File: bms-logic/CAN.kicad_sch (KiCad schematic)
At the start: 56 parts, among them J5 Connector, USB-TYPE-C-16P, J6 Conn_01x04, U10 TCAN334D, U5 MP9485GN-Z, U6 MIE1W0505BGLVH-3R-Z, U7 ISO7041FDBQ, U8 ADUM3160, U9 LTV-217-B-G

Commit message: started afe layout
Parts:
- renumbered C22 to C18, C23 to C19, C24 to C20, C25 to C21, C26 to C22, C27 to C23, C28 to C24, C29 to C25, C30 to C26, C31 to C27, C32 to C28, C33 to C29, C34 to C30, C35 to C31, C36 to C32, C37 to C33, C38 to C34, C39 to C35, J5 to J3, J6 to J4, U8 to U10, U9 to U11, U10 to U12, U5 to U7, U6 to U8, U7 to U9

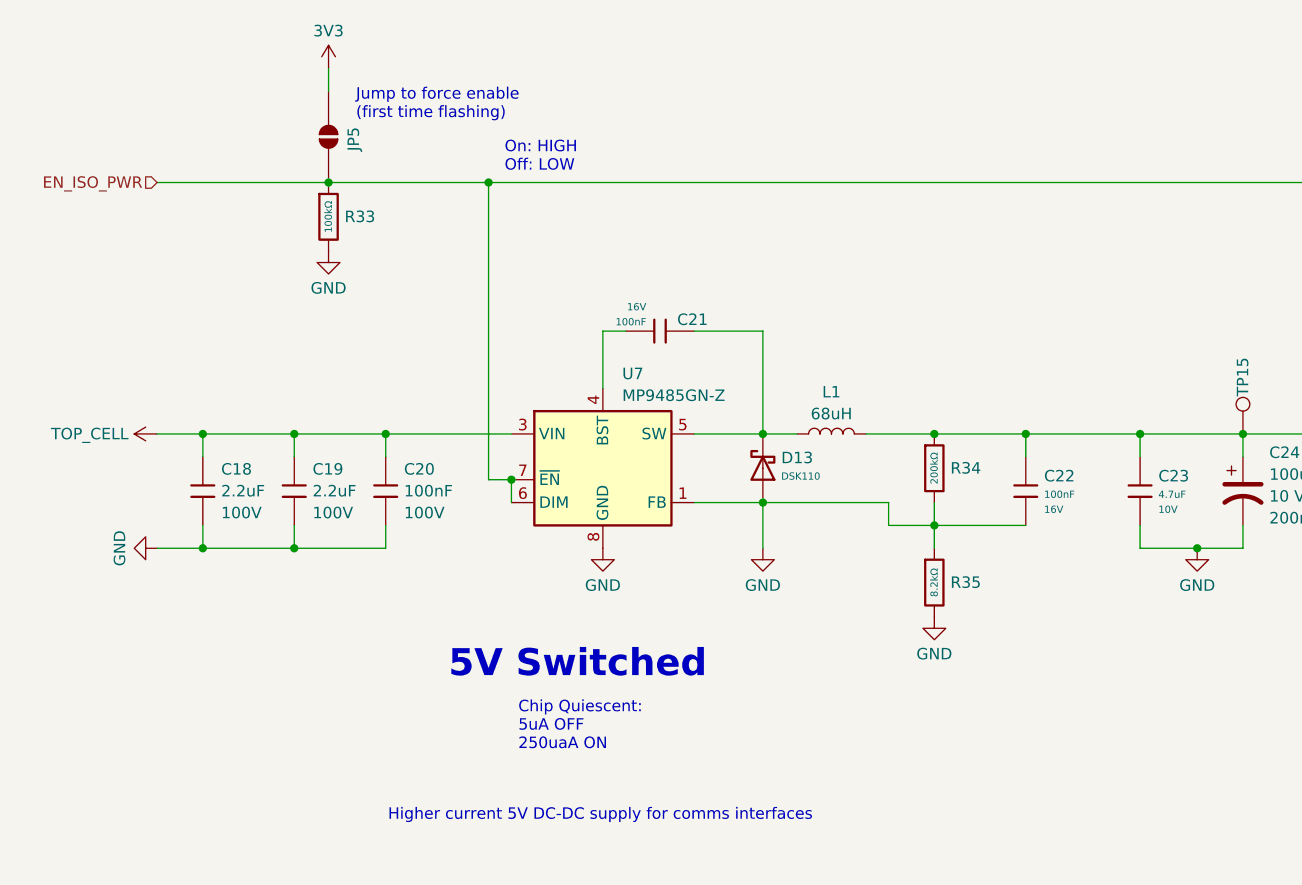
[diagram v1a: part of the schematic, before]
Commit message: power supply layout
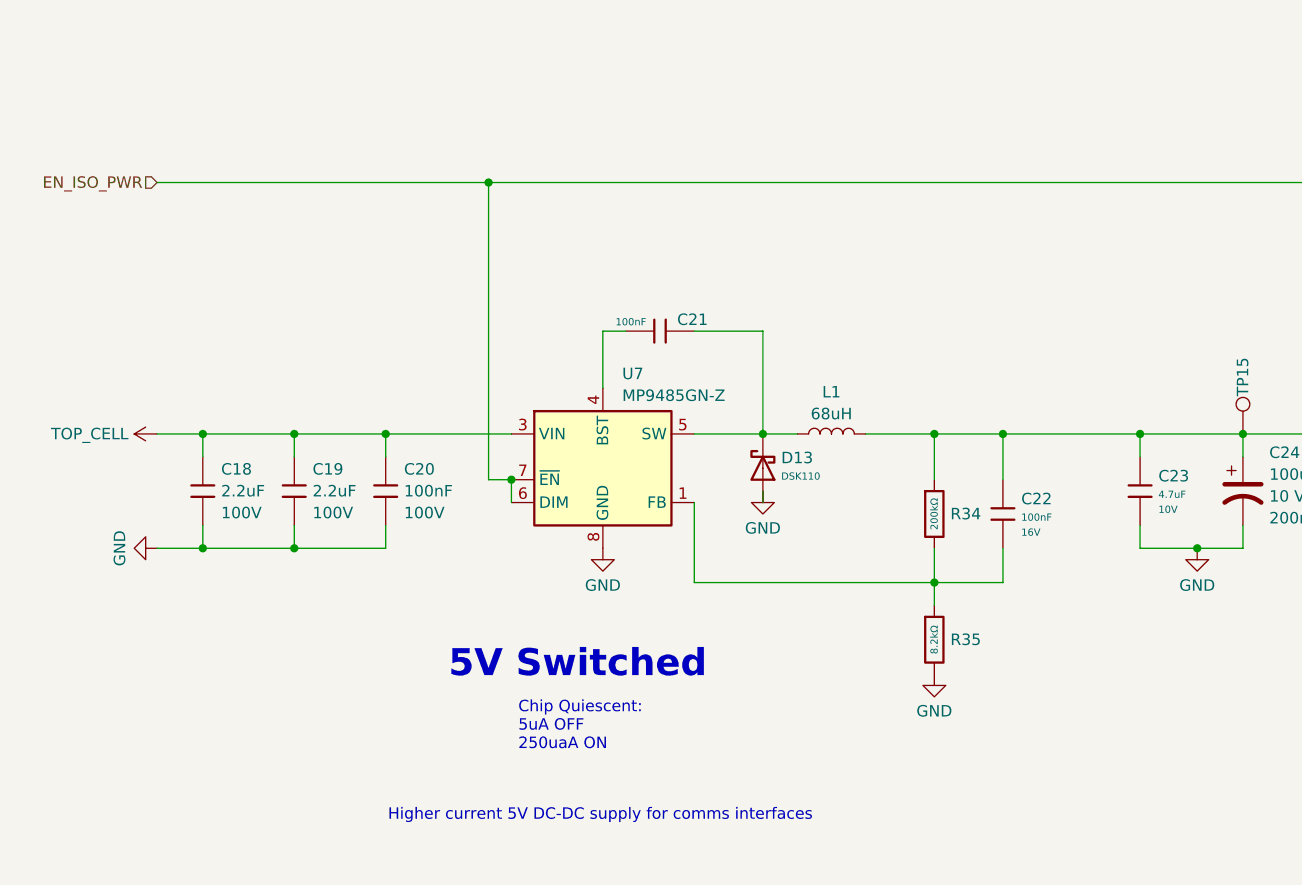
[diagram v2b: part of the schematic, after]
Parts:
- removed JP5: SolderJumper_2_Open, Jumper:SolderJumper-2_P1.3mm_Open_RoundedPad1.0x1.5mm, symbol Jumper:SolderJumper_2_Open
- removed R33: 100kΩ, PCM_JLCPCB:R_0402, symbol PCM_JLCPCB-Resistors:0402,100kΩ
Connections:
- net GND: no longer C22.1, R34.2, R35.1, U7.1 (FB)
- new net: C22.1, R34.2, R35.1, U7.1 (FB)
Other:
- note removed: "Jump to force enable (first time flashing)"
- note removed: "On: HIGH Off: LOW"
- moved on the sheet: C22, R34, R35

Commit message: isolated comms
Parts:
- removed J4: Conn_01x04, symbol Connector_Generic:Conn_01x04
- removed JP6: SolderJumper_2_Open, Jumper:SolderJumper-2_P1.3mm_Open_RoundedPad1.0x1.5mm, symbol Jumper:SolderJumper_2_Open
- added C54, C55: 100nF, PCM_JLCPCB:C_0402, symbol PCM_JLCPCB-Capacitors:0402,100nF
- added CN5: S4B-ZR-SM4A-TF_LF_SN, Connector_JST:JST_ZH_S4B-ZR-SM4A-TF_1x04-1MP_P1.50mm_Horizontal, symbol JLCImport:S4B-ZR-SM4A-TF_LF_SN
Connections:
- net 3V3: now also C54.1
- net 5V0_ISO_SW: now also C55.1, CN5.1
- net GND: now also C54.2; no longer C31.1
- net GNDISO: now also C31.1, C55.2, CN5.4, CN5.5, CN5.6
- net at D15.1 (K), R47.1, U12.7 (CANH): now also CN5.2
- net at D15.2 (K), JP7.1 (A), U12.6 (CANL): now also CN5.3
- no-connect marks 5 -> 6
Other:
- moved on the sheet: TP16, TP17, TP18, TP19

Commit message: diagonal
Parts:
- CN5: footprint Connector_JST:JST_ZH_S4B-ZR-SM4A-TF_1x04-1MP_P1.50mm_Horizontal -> JLCImport:JST_ZH_S4B-ZR-SM4A-TF_1x04-1MP_P1.50mm_Horizontal
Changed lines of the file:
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@@
 			)
 		)
-		(property "Footprint" "Connector_JST:JST_ZH_S4B-ZR-SM4A-TF_1x04-1MP_P1.50mm_Horizontal"
+		(property "Footprint" "JLCImport:JST_ZH_S4B-ZR-SM4A-TF_1x04-1MP_P1.50mm_Horizontal"
 			(at 388.62 119.38 0)
 			(hide yes)

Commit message: kicad 10.0.1 before update to .2
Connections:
- net GNDISO: now also CN5.MP (5); no longer CN5.5, CN5.6
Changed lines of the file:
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@@
 		(pin "3"
 		)
-		(pin "6"
+		(pin "MP"
 		)
 		(pin "2"
@@
 		(pin "1"
 		)
-		(pin "5"
+		(pin "MP"
 		)
 		(instances

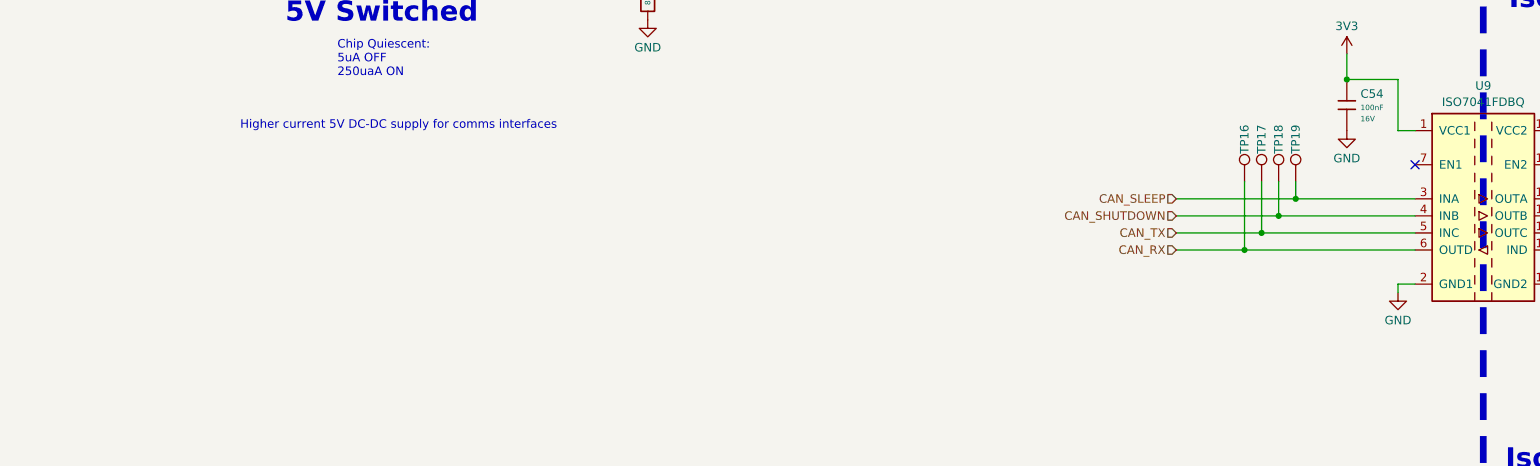
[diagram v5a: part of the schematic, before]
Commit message: more layout, removed some unnecessary features
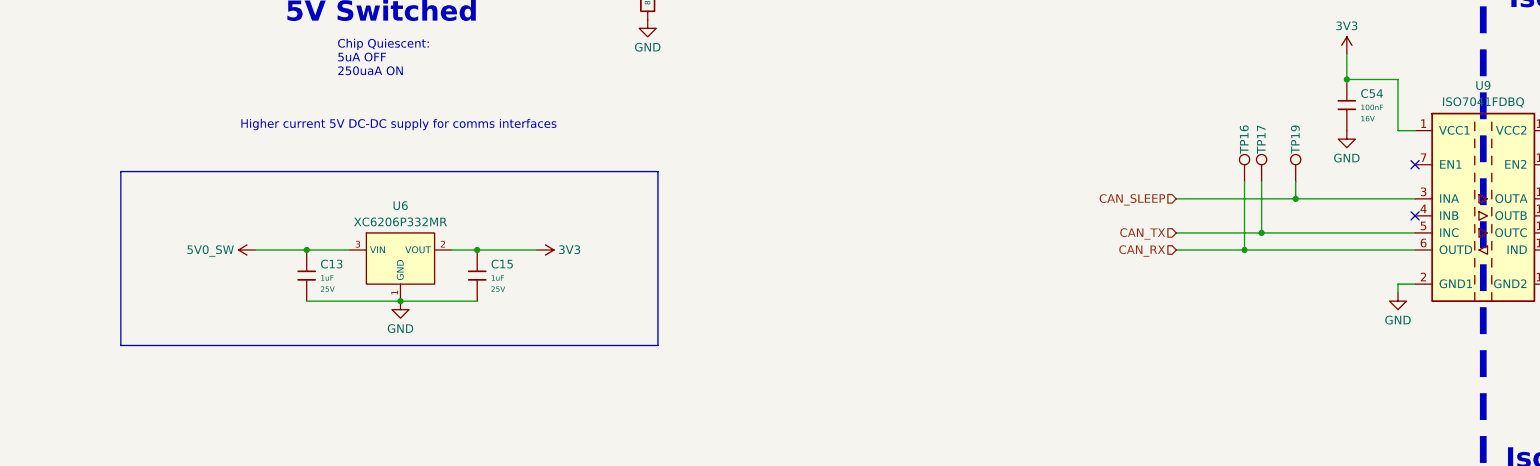
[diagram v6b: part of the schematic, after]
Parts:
- removed TP18: IO8, TestPoint:TestPoint_Pad_D1.0mm, symbol Connector:TestPoint
- added C13, C15: 1uF, PCM_JLCPCB:C_0402, symbol PCM_JLCPCB-Capacitors:0402,1uF
- added U6: XC6206P332MR, PCM_JLCPCB:SOT-23-3_L2.9-W1.6-P1.90-LS2.8-BR, symbol PCM_JLCPCB-Power:LDO, 3.3V, 0.2A
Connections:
- net 3V3: now also C15.1, U6.2 (VOUT)
- net 5V0_SW: now also C13.1, U6.3 (VIN)
- net GND: now also C13.2, C15.2, U6.1 (GND)
- net CAN_SHUTDOWN: no longer names the net of U9.4 (INB)
- no-connect marks 6 -> 7

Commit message: done with layout, need to address some DRC
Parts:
- renumbered CN5 to CN7, J3 to CN8
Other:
- note added: "change sch symbool to CN?"
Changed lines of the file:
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@@
 		)
 	)
+	(text "change sch symbool to CN?"
+		(exclude_from_sim no)
+		(at 357.632 184.658 0)
+		(effects
+			(font
+				(size 1.27 1.27)
+			)
+		)
+	)
 	(text "Isolated CANbus 2.0B Interface"
 		(exclude_from_sim no)
@@
 		(in_pos_files yes)
 		(dnp no)
-		(property "Reference" "CN5"
+		(property "Reference" "CN7"
 			(at 378.714 135.4977 0)
 			(show_name no)
@@
 			(project "battery-node"
 				(path "/0531bb65-44fe-462a-8fbf-92fb22c9abe0/a0e287d3-b915-410a-86a7-dfb59e4205a2"
-					(reference "CN5")
+					(reference "CN7")
 					(unit 1)
 				)
@@
 		(in_pos_files yes)
 		(dnp no)
-		(property "Reference" "J3"
+		(property "Reference" "CN8"
 			(at 328.93 176.0799 0)
 			(show_name no)
@@
 			(project "battery-node"
 				(path "/0531bb65-44fe-462a-8fbf-92fb22c9abe0/a0e287d3-b915-410a-86a7-dfb59e4205a2"
-					(reference "J3")
+					(reference "CN8")
 					(unit 1)
 				)
